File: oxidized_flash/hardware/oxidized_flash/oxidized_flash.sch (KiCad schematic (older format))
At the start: 13 parts

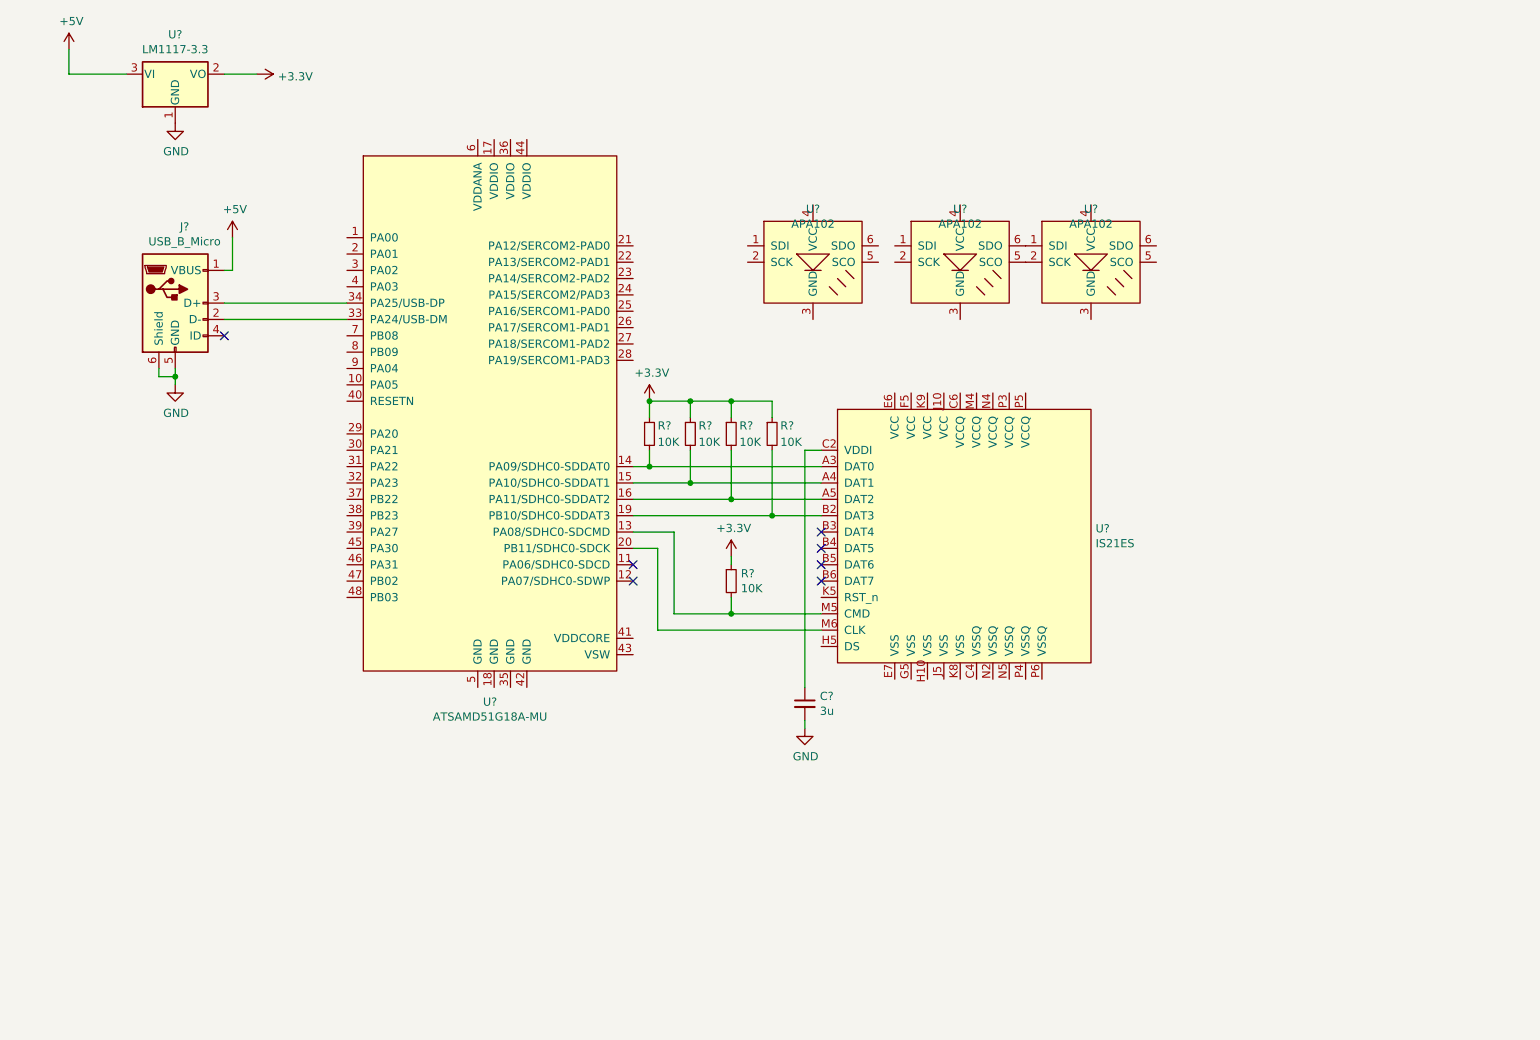
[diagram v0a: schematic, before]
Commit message: First schematic draft without battery or OLED screen
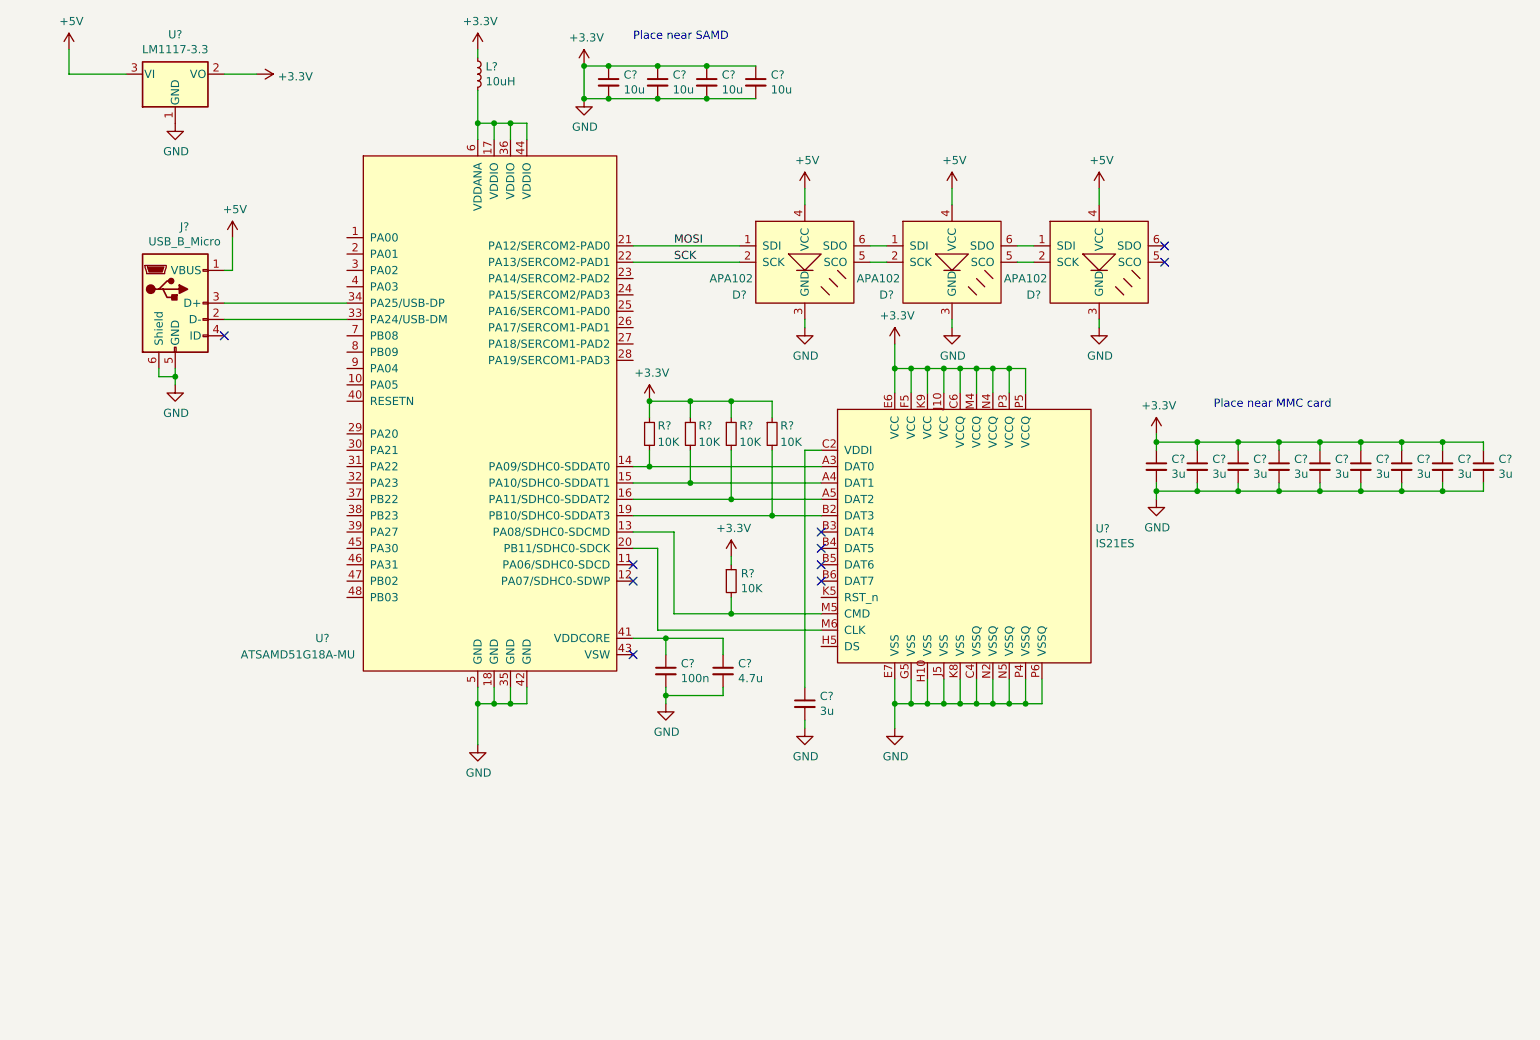
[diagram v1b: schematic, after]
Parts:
- removed U? (x3): APA102, symbol Custom_LED:APA102
- removed U?: ATSAMD51G18A-MU, symbol ATSAMD:ATSAMD51G18A-MU
- added C? (x4): 10u, symbol Device:C_Small
- added C?: 4.7u, symbol Device:C_Small
- added C?: 100n, symbol Device:C_Small
- added C? (x9): 3u, symbol Device:C_Small
- added D? (x3): APA102, symbol Custom_LED:APA102
- added L?: 10uH, symbol Device:L_Small
- added U?: ATSAMD51G18A-MU, symbol ATSAMD:ATSAMD51G18A-MU
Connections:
- net GND is gone; now on net +3V3: C?.2, J?.5 (GND), J?.6 (Shield), U?.1 (GND)
- net +3V3: now also U?.C4 (VSSQ), U?.C6 (VCCQ), U?.E6 (VCC), U?.E7 (VSS), U?.F5 (VCC), U?.G5 (VSS), U?.H10 (VSS), U?.J10 (VCC), U?.J5 (VSS), U?.K8 (VSS), U?.K9 (VCC), U?.M4 (VCCQ), U?.N2 (VSSQ), U?.N4 (VCCQ), U?.N5 (VSSQ), U?.P3 (VCCQ), U?.P4 (VSSQ), U?.P5 (VCCQ), U?.P6 (VSSQ), C?.1, C?.1, C?.1, C?.1, C?.1, C?.1, C?.1, C?.1, C?.1, C?.1, C?.1, C?.1, C?.1, C?.2, C?.2, C?.2, C?.2, C?.2, C?.2, C?.2, C?.2, C?.2, C?.2, C?.2, C?.2, C?.2, C?.2, C?.2, D?.3 (GND), D?.3 (GND), D?.3 (GND), L?.1, U?.18 (GND), U?.35 (GND), U?.42 (GND), U?.5 (GND)
- net +5V: now also D?.4 (VCC), D?.4 (VCC), D?.4 (VCC)
- net at J?.2 (D-): now also U?.33 (PA24/USB-DM)
- net at J?.3 (D+): now also U?.34 (PA25/USB-DP)
- net at R?.2, U?.A3 (DAT0): now also U?.14 (PA09/SDHC0-SDDAT0)
- net at R?.2, U?.A4 (DAT1): now also U?.15 (PA10/SDHC0-SDDAT1)
- net at R?.2, U?.A5 (DAT2): now also U?.16 (PA11/SDHC0-SDDAT2)
- net at R?.2, U?.B2 (DAT3): now also U?.19 (PB10/SDHC0-SDDAT3)
- net at R?.2, U?.M5 (CMD): now also U?.13 (PA08/SDHC0-SDCMD)
- net at U?.M6 (CLK): now also U?.20 (PB11/SDHC0-SDCK)
- new net: L?.2, U?.17 (VDDIO), U?.36 (VDDIO), U?.44 (VDDIO), U?.6 (VDDANA)
- new net: C?.1, C?.1, U?.41 (VDDCORE)
- new net: D?.2 (SCK), D?.5 (SCO) (x2)
- new net: D?.1 (SDI), D?.6 (SDO) (x2)
- new net MOSI: D?.1 (SDI), U?.21 (PA12/SERCOM2-PAD0)
- new net SCK: D?.2 (SCK), U?.22 (PA13/SERCOM2-PAD1)
- no-connect marks 7 -> 10
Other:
- note added: "Place near MMC card"
- note added: "Place near SAMD"

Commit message: Cleanup schematic before battery power work
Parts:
- removed L?: 10uH, symbol Device:L_Small
- added C? (x2): 22p, symbol Device:C_Small
- added C?: 0.1u, symbol Device:C_Small
- added D?: LED_Small, symbol Device:LED_Small
- added F?: 500mA, symbol Device:Fuse_Small
- added L?: 10uH, symbol Device:L_Small
- added R?: 10k, symbol Device:R_Small
- added R?: R_Small, symbol Device:R_Small
- added Y?: 32.768, symbol Device:Crystal_Small
- C?: value 4.7u -> 0.1u
- C?: value 100n -> 4.7u
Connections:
- net +3V3: now also U?.17 (VDDIO), U?.36 (VDDIO), U?.44 (VDDIO), U?.6 (VDDANA), C?.2, C?.2, C?.2, R?.1, R?.2
- net +5V: now also F?.1; no longer U?.3 (VI)
- net at U?.1 (PA00): now also C?.1, Y?.1
- net at U?.2 (PA01): now also C?.1, Y?.2
- net PA20: now reaches U?.29 (PA20)
- net PA20: now also D?.2 (A)
- net at U?.40 (RESETN): now also C?.1, R?.2
- net at C?.1, C?.1, U?.41 (VDDCORE): now also L?.2
- net at U?.43 (VSW): now also L?.1
- new net: F?.2, U?.3 (VI)
- new net: D?.1 (K), R?.1
- no-connect marks 10 -> 9
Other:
- moved on the sheet: C?

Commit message: Add annotations
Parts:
- gave numbers to parts that had none: 37

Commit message: Assign footprints to some of the schematic
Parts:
- C1, C10, C11, C12, C13, C14, C15, C16, C17, C18, C19, C2, C3, C4, C5, C6, C7, C8, C9: footprint (none) -> Capacitor_SMD:C_0805_2012Metric
- D1: footprint (none) -> LED_SMD:LED_0805_2012Metric
- R1: value R_Small -> 1k; footprint (none) -> Resistor_SMD:R_0805_2012Metric
- R2, R3, R4, R5, R6, R7: footprint (none) -> Resistor_SMD:R_0805_2012Metric
- U2: footprint (none) -> Package_DFN_QFN:QFN-48-1EP_7x7mm_P0.5mm_EP5.3x5.3mm
- U3: footprint (none) -> Custom_BGA:FBGA-153_14x14_11.5x13.0mm
- Y1: footprint (none) -> Custom_Crystal:ECS-31B_xtal
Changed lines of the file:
@@
 F 0 "U3" H 7228 4221 50  0000 L CNN
 F 1 "IS21ES" H 7228 4130 50  0000 L CNN
-F 2 "" H 6000 4100 50  0001 C CNN
+F 2 "Custom_BGA:FBGA-153_14x14_11.5x13.0mm" H 6000 4100 50  0001 C CNN
 F 3 "" H 6000 4100 50  0001 C CNN
 	1    6000 4100
@@
 F 0 "R3" H 4550 3450 50  0000 L CNN
 F 1 "10K" H 4550 3350 50  0000 L CNN
-F 2 "" H 4500 3400 50  0001 C CNN
+F 2 "Resistor_SMD:R_0805_2012Metric" H 4500 3400 50  0001 C CNN
 F 3 "~" H 4500 3400 50  0001 C CNN
 	1    4500 3400
@@
 F 0 "R4" H 4800 3450 50  0000 L CNN
 F 1 "10K" H 4800 3350 50  0000 L CNN
-F 2 "" H 4750 3400 50  0001 C CNN
+F 2 "Resistor_SMD:R_0805_2012Metric" H 4750 3400 50  0001 C CNN
 F 3 "~" H 4750 3400 50  0001 C CNN
 	1    4750 3400
@@
 F 0 "R5" H 5050 3450 50  0000 L CNN
 F 1 "10K" H 5050 3350 50  0000 L CNN
-F 2 "" H 5000 3400 50  0001 C CNN
+F 2 "Resistor_SMD:R_0805_2012Metric" H 5000 3400 50  0001 C CNN
 F 3 "~" H 5000 3400 50  0001 C CNN
 	1    5000 3400
@@
 F 0 "R7" H 5300 3450 50  0000 L CNN
 F 1 "10K" H 5300 3350 50  0000 L CNN
-F 2 "" H 5250 3400 50  0001 C CNN
+F 2 "Resistor_SMD:R_0805_2012Metric" H 5250 3400 50  0001 C CNN
 F 3 "~" H 5250 3400 50  0001 C CNN
 	1    5250 3400
@@
 F 0 "R6" H 5059 4346 50  0000 L CNN
 F 1 "10K" H 5059 4255 50  0000 L CNN
-F 2 "" H 5000 4300 50  0001 C CNN
+F 2 "Resistor_SMD:R_0805_2012Metric" H 5000 4300 50  0001 C CNN
 F 3 "~" H 5000 4300 50  0001 C CNN
 	1    5000 4300
@@
 F 0 "C10" H 5542 5096 50  0000 L CNN
 F 1 "3u" H 5542 5005 50  0000 L CNN
-F 2 "" H 5450 5050 50  0001 C CNN
+F 2 "Capacitor_SMD:C_0805_2012Metric" H 5450 5050 50  0001 C CNN
 F 3 "~" H 5450 5050 50  0001 C CNN
 	1    5450 5050
@@
 F 0 "C4" H 4342 1296 50  0000 L CNN
 F 1 "10u" H 4342 1205 50  0000 L CNN
-F 2 "" H 4250 1250 50  0001 C CNN
+F 2 "Capacitor_SMD:C_0805_2012Metric" H 4250 1250 50  0001 C CNN
 F 3 "~" H 4250 1250 50  0001 C CNN
 	1    4250 1250
@@
 F 0 "C5" H 4642 1296 50  0000 L CNN
 F 1 "10u" H 4642 1205 50  0000 L CNN
-F 2 "" H 4550 1250 50  0001 C CNN
+F 2 "Capacitor_SMD:C_0805_2012Metric" H 4550 1250 50  0001 C CNN
 F 3 "~" H 4550 1250 50  0001 C CNN
 	1    4550 1250
@@
 F 0 "C7" H 4942 1296 50  0000 L CNN
 F 1 "10u" H 4942 1205 50  0000 L CNN
-F 2 "" H 4850 1250 50  0001 C CNN
+F 2 "Capacitor_SMD:C_0805_2012Metric" H 4850 1250 50  0001 C CNN
 F 3 "~" H 4850 1250 50  0001 C CNN
 	1    4850 1250
@@
 F 0 "C9" H 5242 1296 50  0000 L CNN
 F 1 "10u" H 5242 1205 50  0000 L CNN
-F 2 "" H 5150 1250 50  0001 C CNN
+F 2 "Capacitor_SMD:C_0805_2012Metric" H 5150 1250 50  0001 C CNN
 F 3 "~" H 5150 1250 50  0001 C CNN
 	1    5150 1250
@@
 F 0 "U2" H 2500 2050 50  0000 C CNN
 F 1 "ATSAMD51G18A-MU" H 2350 1950 50  0000 C CNN
-F 2 "" H 3600 3350 50  0001 C CNN
+F 2 "Package_DFN_QFN:QFN-48-1EP_7x7mm_P0.5mm_EP5.3x5.3mm" H 3600 3350 50  0001 C CNN
 F 3 "" H 3600 3350 50  0001 C CNN
 	1    3600 3350
@@
 F 0 "C8" H 5192 4896 50  0000 L CNN
 F 1 "0.1u" H 5192 4805 50  0000 L CNN
-F 2 "" H 5100 4850 50  0001 C CNN
+F 2 "Capacitor_SMD:C_0805_2012Metric" H 5100 4850 50  0001 C CNN
 F 3 "~" H 5100 4850 50  0001 C CNN
 	1    5100 4850
@@
 F 0 "C6" H 4842 4896 50  0000 L CNN
 F 1 "4.7u" H 4842 4805 50  0000 L CNN
-F 2 "" H 4750 4850 50  0001 C CNN
+F 2 "Capacitor_SMD:C_0805_2012Metric" H 4750 4850 50  0001 C CNN
 F 3 "~" H 4750 4850 50  0001 C CNN
 	1    4750 4850
@@
 F 0 "C11" H 7692 3646 50  0000 L CNN
 F 1 "3u" H 7692 3555 50  0000 L CNN
-F 2 "" H 7600 3600 50  0001 C CNN
+F 2 "Capacitor_SMD:C_0805_2012Metric" H 7600 3600 50  0001 C CNN
 F 3 "~" H 7600 3600 50  0001 C CNN
 	1    7600 3600
@@
 F 0 "C12" H 7942 3646 50  0000 L CNN
 F 1 "3u" H 7942 3555 50  0000 L CNN
-F 2 "" H 7850 3600 50  0001 C CNN
+F 2 "Capacitor_SMD:C_0805_2012Metric" H 7850 3600 50  0001 C CNN
 F 3 "~" H 7850 3600 50  0001 C CNN
 	1    7850 3600
@@
 F 0 "C13" H 8192 3646 50  0000 L CNN
 F 1 "3u" H 8192 3555 50  0000 L CNN
-F 2 "" H 8100 3600 50  0001 C CNN
+F 2 "Capacitor_SMD:C_0805_2012Metric" H 8100 3600 50  0001 C CNN
 F 3 "~" H 8100 3600 50  0001 C CNN
 	1    8100 3600
@@
 F 0 "C14" H 8442 3646 50  0000 L CNN
 F 1 "3u" H 8442 3555 50  0000 L CNN
-F 2 "" H 8350 3600 50  0001 C CNN
+F 2 "Capacitor_SMD:C_0805_2012Metric" H 8350 3600 50  0001 C CNN
 F 3 "~" H 8350 3600 50  0001 C CNN
 	1    8350 3600
@@
 F 0 "C15" H 8692 3646 50  0000 L CNN
 F 1 "3u" H 8692 3555 50  0000 L CNN
-F 2 "" H 8600 3600 50  0001 C CNN
+F 2 "Capacitor_SMD:C_0805_2012Metric" H 8600 3600 50  0001 C CNN
 F 3 "~" H 8600 3600 50  0001 C CNN
 	1    8600 3600
@@
 F 0 "C16" H 8942 3646 50  0000 L CNN
 F 1 "3u" H 8942 3555 50  0000 L CNN
-F 2 "" H 8850 3600 50  0001 C CNN
+F 2 "Capacitor_SMD:C_0805_2012Metric" H 8850 3600 50  0001 C CNN
 F 3 "~" H 8850 3600 50  0001 C CNN
 	1    8850 3600
@@
 F 0 "C17" H 9192 3646 50  0000 L CNN
 F 1 "3u" H 9192 3555 50  0000 L CNN
-F 2 "" H 9100 3600 50  0001 C CNN
+F 2 "Capacitor_SMD:C_0805_2012Metric" H 9100 3600 50  0001 C CNN
 F 3 "~" H 9100 3600 50  0001 C CNN
 	1    9100 3600
@@
 F 0 "C18" H 9442 3646 50  0000 L CNN
 F 1 "3u" H 9442 3555 50  0000 L CNN
-F 2 "" H 9350 3600 50  0001 C CNN
+F 2 "Capacitor_SMD:C_0805_2012Metric" H 9350 3600 50  0001 C CNN
 F 3 "~" H 9350 3600 50  0001 C CNN
 	1    9350 3600
@@
 F 0 "C19" H 9692 3646 50  0000 L CNN
 F 1 "3u" H 9692 3555 50  0000 L CNN
-F 2 "" H 9600 3600 50  0001 C CNN
+F 2 "Capacitor_SMD:C_0805_2012Metric" H 9600 3600 50  0001 C CNN
 F 3 "~" H 9600 3600 50  0001 C CNN
 	1    9600 3600
@@
 F 0 "Y1" V 2304 2338 50  0000 L CNN
 F 1 "32.768" V 2400 2300 50  0000 L CNN
-F 2 "" H 2350 2250 50  0001 C CNN
+F 2 "Custom_Crystal:ECS-31B_xtal" H 2350 2250 50  0001 C CNN
 F 3 "~" H 2350 2250 50  0001 C CNN
 	1    2350 2250
@@
 F 0 "C1" V 1971 2150 50  0000 C CNN
 F 1 "22p" V 2050 2150 50  0000 C CNN
-F 2 "" H 2200 2150 50  0001 C CNN
+F 2 "Capacitor_SMD:C_0805_2012Metric" H 2200 2150 50  0001 C CNN
 F 3 "~" H 2200 2150 50  0001 C CNN
 	1    2200 2150
@@
 F 0 "C2" V 2300 2450 50  0000 C CNN
 F 1 "22p" V 2350 2350 50  0000 C CNN
-F 2 "" H 2200 2350 50  0001 C CNN
+F 2 "Capacitor_SMD:C_0805_2012Metric" H 2200 2350 50  0001 C CNN
 F 3 "~" H 2200 2350 50  0001 C CNN
 	1    2200 2350
@@
 F 0 "R2" H 2259 3096 50  0000 L CNN
 F 1 "10k" H 2259 3005 50  0000 L CNN
-F 2 "" H 2200 3050 50  0001 C CNN
+F 2 "Resistor_SMD:R_0805_2012Metric" H 2200 3050 50  0001 C CNN
 F 3 "~" H 2200 3050 50  0001 C CNN
 	1    2200 3050
@@
 F 0 "C3" H 2292 3446 50  0000 L CNN
 F 1 "0.1u" H 2292 3355 50  0000 L CNN
-F 2 "" H 2200 3400 50  0001 C CNN
+F 2 "Capacitor_SMD:C_0805_2012Metric" H 2200 3400 50  0001 C CNN
 F 3 "~" H 2200 3400 50  0001 C CNN
 	1    2200 3400
@@
 P 1050 4450
 F 0 "R1" H 1109 4496 50  0000 L CNN
-F 1 "R_Small" H 1109 4405 50  0000 L CNN
-F 2 "" H 1050 4450 50  0001 C CNN
+F 1 "1k" H 1109 4405 50  0000 L CNN
+F 2 "Resistor_SMD:R_0805_2012Metric" H 1050 4450 50  0001 C CNN
 F 3 "~" H 1050 4450 50  0001 C CNN
 	1    1050 4450
@@
 F 0 "D1" V 1096 4082 50  0000 R CNN
 F 1 "LED_Small" V 1005 4082 50  0000 R CNN
-F 2 "" V 1050 4150 50  0001 C CNN
+F 2 "LED_SMD:LED_0805_2012Metric" V 1050 4150 50  0001 C CNN
 F 3 "~" V 1050 4150 50  0001 C CNN
 	1    1050 4150

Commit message: Add initial schematic, and SWD interface
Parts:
- removed D4: APA102, symbol Custom_LED:APA102
- added J?: Conn_ARM_JTAG_SWD_10, Connector_PinHeader_1.27mm:PinHeader_2x05_P1.27mm_Vertical_SMD, symbol Connector:Conn_ARM_JTAG_SWD_10
- added R?: 10k, symbol Device:R_Small
- D2, D3: footprint (none) -> Custom_LED:APA102-2020
- F1: footprint (none) -> Fuse:Fuse_0805_2012Metric
- J1: footprint (none) -> Custom_USB:USB-MICRO-B-FCI-10118192
- L1: footprint (none) -> Inductor_SMD:L_0805_2012Metric
- U1: footprint (none) -> Package_TO_SOT_SMD:SOT-223
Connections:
- net +3V3: now also J?.1 (VCC), J?.3 (GND), J?.5 (GND), J?.9 (GNDDetect), R?.1
- net SWD_RST: now reaches C3.1, R2.2, U2.40 (RESETN)
- net SWD_RST: now also J?.10 (~RESET~)
- net SWD_CLK: now reaches U2.45 (PA30)
- net SWD_CLK: now also J?.4 (SWDCLK/TCK), R?.2
- net SWD_IO: now reaches U2.46 (PA31)
- net SWD_IO: now also J?.2 (SWDIO/TMS)
- no-connect marks 9 -> 11

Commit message: Remove crystal
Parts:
- removed C1, C2: 22p, Capacitor_SMD:C_0805_2012Metric, symbol Device:C_Small
- removed Y1: 32.768, Custom_Crystal:ECS-31B_xtal, symbol Device:Crystal_Small
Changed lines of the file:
@@
 SCK
-Wire Wire Line
-	2650 2200 2650 2150
-Wire Wire Line
-	2650 2300 2650 2350
-Wire Wire Line
-	2100 2150 2000 2150
-Wire Wire Line
-	2000 2150 2000 2350
-Wire Wire Line
-	2100 2350 2000 2350
-Connection ~ 2000 2350
-Wire Wire Line
-	2000 2350 2000 2450
-$Comp
-L power:GND #PWR06
-U 1 1 5C4E574A
-P 2000 2450
-F 0 "#PWR06" H 2000 2200 50  0001 C CNN
-F 1 "GND" H 2005 2277 50  0001 C CNN
-F 2 "" H 2000 2450 50  0001 C CNN
-F 3 "" H 2000 2450 50  0001 C CNN
-	1    2000 2450
-	1    0    0    -1
-$EndComp
 Wire Wire Line
 	1950 1950 1950 2400
@@
 Text Label 1850 3200 0    50   ~ 0
 SWD_RST
-$Comp
-L Device:C_Small C2
-U 1 1 5C4CF009
-P 2200 2350
-F 0 "C2" V 2300 2450 50  0000 C CNN
-F 1 "22p" V 2350 2350 50  0000 C CNN
-F 2 "Capacitor_SMD:C_0805_2012Metric" H 2200 2350 50  0001 C CNN
-F 3 "~" H 2200 2350 50  0001 C CNN
-	1    2200 2350
-	0    1    1    0
-$EndComp
-Wire Wire Line
-	2350 2350 2300 2350
-Wire Wire Line
-	2650 2350 2350 2350
-Connection ~ 2350 2350
-Wire Wire Line
-	2350 2150 2300 2150
-Wire Wire Line
-	2650 2150 2350 2150
-Connection ~ 2350 2150
-$Comp
-L Device:Crystal_Small Y1
-U 1 1 5C4B1D39
-P 2350 2250
-F 0 "Y1" V 2304 2338 50  0000 L CNN
-F 1 "32.768" V 2400 2300 50  0000 L CNN
-F 2 "Custom_Crystal:ECS-31B_xtal" H 2350 2250 50  0001 C CNN
-F 3 "~" H 2350 2250 50  0001 C CNN
-	1    2350 2250
-	0    1    1    0
-$EndComp
-$Comp
-L Device:C_Small C1
-U 1 1 5C4CE74A
-P 2200 2150
-F 0 "C1" V 1971 2150 50  0000 C CNN
-F 1 "22p" V 2050 2150 50  0000 C CNN
-F 2 "Capacitor_SMD:C_0805_2012Metric" H 2200 2150 50  0001 C CNN
-F 3 "~" H 2200 2150 50  0001 C CNN
-	1    2200 2150
-	0    1    1    0
-$EndComp
 $EndSCHEMATC
